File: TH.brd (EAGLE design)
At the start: 129.5 x 71.1 mm, 57 parts, among them IC1 TLE5205-2, IC2 TLE5205-2, IC3 TLE5205-2, IC5 TLE5205-2, J1 I2C, J3 POWERPOLE_DOUBLE, M0 Motor3, M1 Motor3, M2 Motor3, M3 Motor3, U1 LM2576.SMD

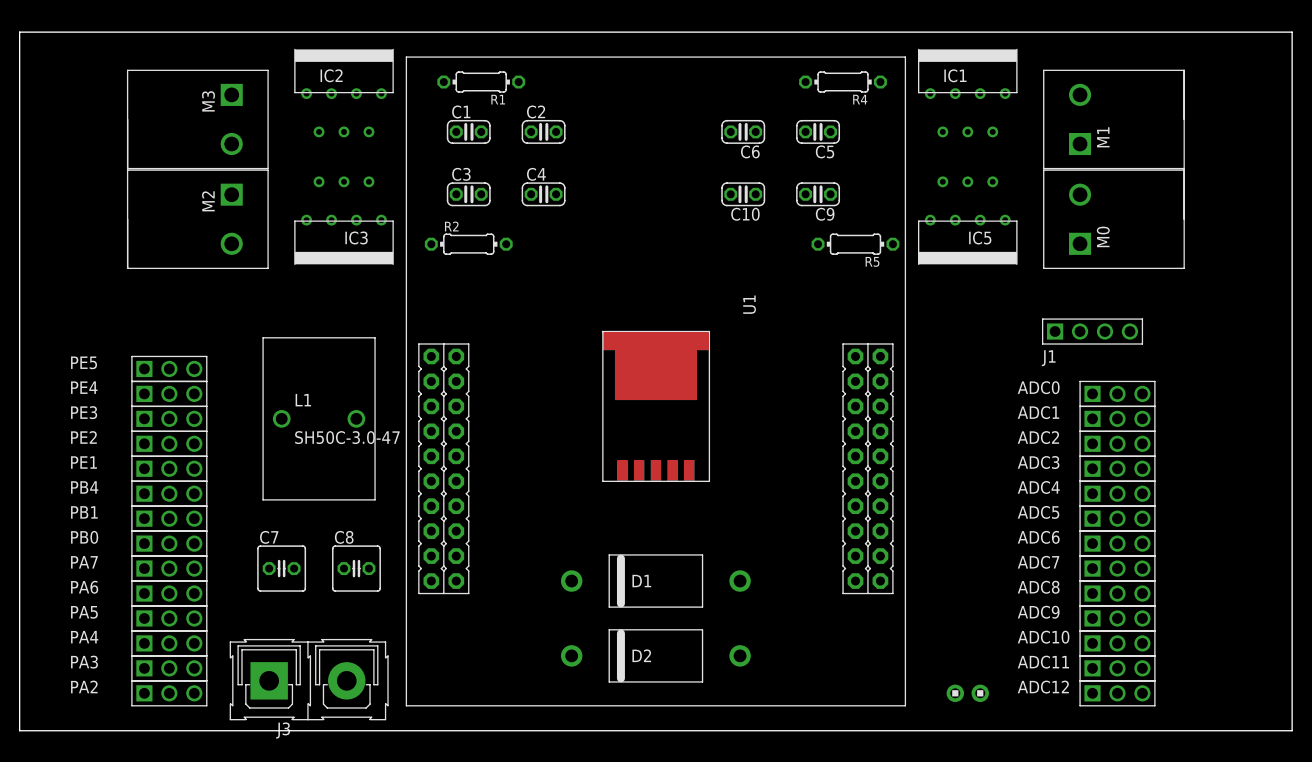
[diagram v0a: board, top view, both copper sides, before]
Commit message: Finished Traces
Only thing left to do is label everything, and ground layer, with do
this tomorrow after TRR
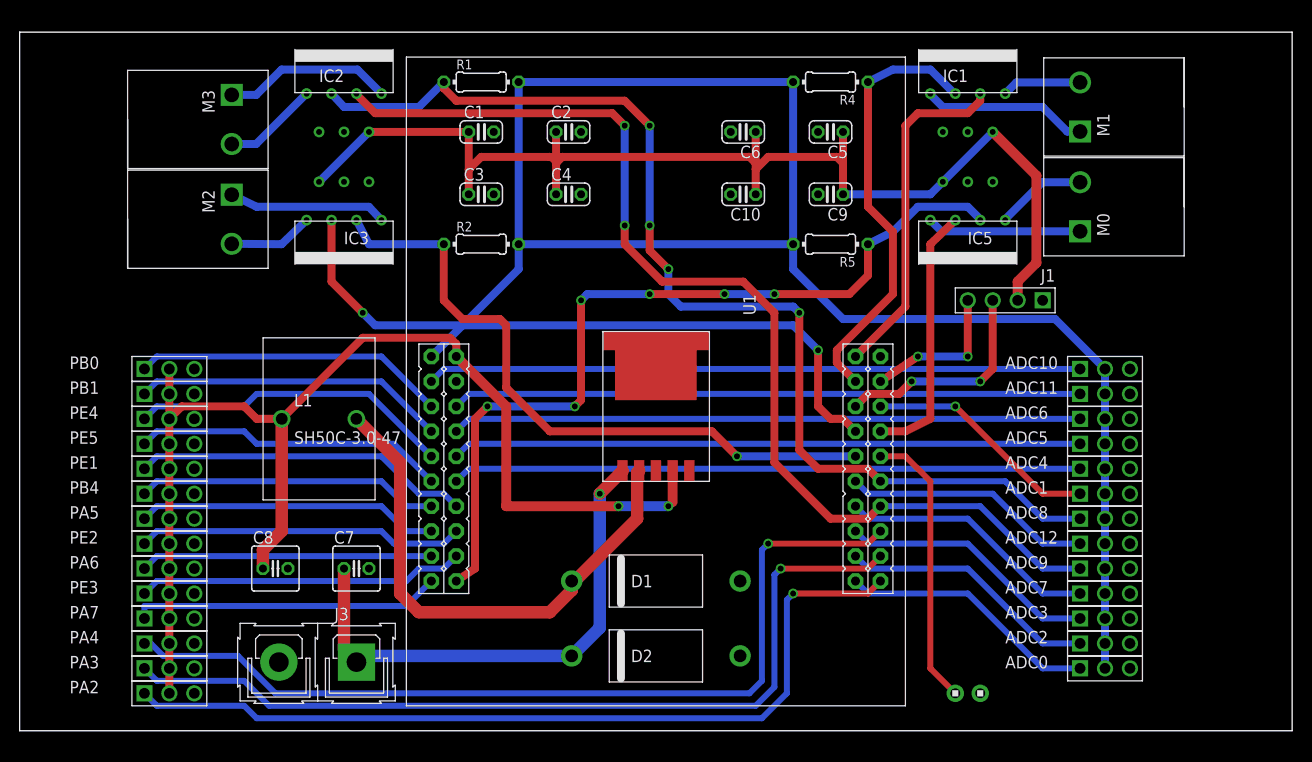
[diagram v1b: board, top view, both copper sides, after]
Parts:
- moved ADC0 28.0 mm to (95.2, 3.81)
- moved ADC11 28.0 mm to (95.2, 31.8)
- moved ADC10 28.0 mm to (95.2, 34.3)
- moved ADC2 20.4 mm to (95.2, 6.35)
- moved PE3 17.8 mm to (0.00, 11.4)
- moved PB0 17.8 mm to (0.00, 34.3)
- moved ADC12 15.3 mm to (95.2, 16.5)
- moved ADC3 15.3 mm to (95.2, 8.89)
- moved ADC6 12.8 mm to (95.2, 29.2)
- moved PB1 12.7 mm to (0.00, 31.8)
- moved PA5 10.2 mm to (0.00, 19.1)
- moved PE2 10.2 mm to (0.00, 16.5)
- moved J1 9.44 mm to (87.6, 41.3), turned to 180 degrees
- moved J3 9.09 mm to (21.6, 4.45), turned to 180 degrees
- moved C8 8.25 mm to (13.3, 14.0)
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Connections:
- removed net -GND: ADC0.3, ADC1.3, ADC10.3, ADC11.3, ADC12.3, ADC2.3, ADC3.3, ADC4.3, ADC5.3, ADC6.3, ADC7.3, ADC8.3, ADC9.3, C1.2, C10.2, C2.2, C3.2, C4.2, C5.2, C6.2, C7.2, C8.2, C9.2, D1.2, D2.2, J3.2, PA2.3, PA3.3, PA4.3, PA5.3, PA6.3, PA7.3, PB0.3, PB1.3, PB4.3, PE1.3, PE2.3, PE3.3, PE4.3, PE5.3, U$1.GND1, U$1.GND2, U$2.2, U1.3, U1.5, U1.GROUND, U1.GROUND@1
- removed net N$10: J1.1
- removed net N$14: ADC11.1
- removed net N$15: ADC12.1
- net GND: now also ADC0.3, ADC1.3, ADC10.3, ADC11.3, ADC12.3, ADC2.3, ADC3.3, ADC4.3, ADC5.3, ADC6.3, ADC7.3, ADC8.3, ADC9.3, C1.2, C10.2, C2.2, C3.2, C4.2, C5.2, C6.2, C7.2, C8.2, C9.2, D1.2, D2.2, IC5.4, J1.1, J3.2, PA2.3, PA3.3, PA4.3, PA5.3, PA6.3, PA7.3, PB0.3, PB1.3, PB4.3, PE1.3, PE2.3, PE3.3, PE4.3, PE5.3, U$1.GND1, U$1.GND2, U$2.2, U1.3, U1.5, U1.GROUND, U1.GROUND@1
- net PC6: now also ADC12.1
- net PD0: now also ADC11.1
- net V+: no longer C1.1, C10.1, C2.1, C3.1, C4.1, C5.1, C6.1, C9.1, IC1.6, IC3.6
- net VBUS: now also C1.1, C10.1, C2.1, C3.1, C4.1, C5.1, C6.1, C9.1, IC1.6, IC2.6, IC3.6, IC5.6
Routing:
- net VBUS: track 0.00 -> 242.5 mm, vias 0 -> 2
- net +3V3: track 0.00 -> 173.6 mm
- net PB7: track 0.00 -> 113.7 mm, vias 0 -> 4
- net PB6: track 0.00 -> 110.8 mm, vias 0 -> 2
- net PA4: track 0.00 -> 91.7 mm, vias 0 -> 1
- net PA3: track 0.00 -> 89.5 mm, vias 0 -> 1
- net PA2: track 0.00 -> 87.3 mm, vias 0 -> 1
- net PF1: track 0.00 -> 86.1 mm, vias 0 -> 6
- net PC4: track 0.00 -> 69.3 mm, vias 0 -> 2
- net PC5: track 0.00 -> 68.3 mm, vias 0 -> 1
- net PB5: track 0.00 -> 66.6 mm
- net PD3: track 0.00 -> 64.0 mm
- net PD2: track 0.00 -> 64.0 mm
- net PD1: track 0.00 -> 64.0 mm
- net PD0: track 0.00 -> 64.0 mm
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
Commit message: Final Design
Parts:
- removed ADC0, ADC3: 3PINHEADER, RASEagleLib:3PINHEADER
- removed M0, M1: Motor3, RASEagleLib:PHOENIXSCREWTERMINAL_2
- added D3: D2, RASEagleLib:DIODE_17MM
- added PF1: PF0, RASEagleLib:PHOENIXSCREWTERMINAL_2
- added PF2: PF3, RASEagleLib:PHOENIXSCREWTERMINAL_2
- added R3, R6: 10K, resistor:0204/7
- PB7: value Motor3 -> PB6
- PC4: value Motor3 -> PC5
- moved PA2 95.6 mm to (95.2, 8.89)
- renumbered ADC1 to PE0, ADC10 to PB5, ADC11 to PD0, ADC12 to PC7, ADC2 to PF4, ADC4 to PD3, ADC5 to PD2, ADC6 to PD1, ADC7 to PD7, ADC8 to PC6, ADC9 to PD6, M2 to PC4, M3 to PB7
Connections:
- removed net +3V3: ADC0.2, ADC3.2, PB5.2, PC6.2, PC7.2, PD0.2, PD1.2, PD2.2, PD3.2, PD6.2, PD7.2, PE0.2, PF4.2, R1.2, R2.2, R4.2, R5.2, U$1.3.3V
- new net 3.3V: J1.2, PA2.2, PB5.2, PC6.2, PC7.2, PD0.2, PD1.2, PD2.2, PD3.2, PD6.2, PD7.2, PE0.2, PF4.2, R3.2, R6.2, U$1.3.3V
- new net N$5$: C8.1, D3.2, L1.P$2, U1.4
- net GND: now also R1.2, R2.2, R4.2, R5.2; no longer ADC0.3, ADC3.3, PA2.3
- net N$12: now also PF1.2; no longer M0.2
- net N$13: now also PF1.1; no longer M0.1
- net N$7: now also PF2.1; no longer M1.1
- net N$8: now also PF2.2; no longer M1.2
- net PB2: now also R6.1
- net PB3: now also R3.1
- net PB6: no longer PD6.1
- net PB7: no longer PC6.1
- net PC6: now also PC6.1; no longer PC7.1
- net PC7: now also PC7.1; no longer PD7.1
- net PD6: now also PD6.1; no longer ADC3.1
- net PD7: now also PD7.1; no longer PF4.1
- net PF4: now also PF4.1; no longer ADC0.1
- net V+: now also C1.1, C10.1, C2.1, C3.1, C4.1, C5.1, C6.1, C9.1, IC1.6, IC2.6, IC3.6, IC5.6
- net VBUS: now also D3.1; no longer C1.1, C10.1, C2.1, C3.1, C4.1, C5.1, C6.1, C8.1, C9.1, IC1.6, IC2.6, IC3.6, IC5.6, J1.2, L1.P$2, PA2.2, U1.4
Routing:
- net +3V3: track 173.6 -> 0.00 mm
- net VBUS: track 242.5 -> 70.5 mm, vias 2 -> 1
- net V+: track 53.2 -> 203.4 mm, vias 1 -> 3
- net 3.3V: track 0.00 -> 123.2 mm
- net N$5$: track 0.00 -> 73.3 mm, vias 0 -> 2
- net PA2: track 87.3 -> 21.9 mm, vias 1 -> 0
- net PB6: track 110.8 -> 87.8 mm
- net PB7: track 113.7 -> 91.9 mm
- net PB3: track 22.5 -> 24.6 mm
- net PD6: track 26.5 -> 24.4 mm
- net PC7: track 26.5 -> 24.4 mm
- net PD7: track 26.5 -> 24.4 mm
- net N$13: track 15.7 -> 17.5 mm
- net N$7: track 16.9 -> 18.7 mm
- net PD0: track 64.0 -> 65.1 mm, vias 0 -> 2
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- added copper zone on layer 1, net GND
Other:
- board size 129.5 x 71.1 mm -> 118.7 x 72.4 mm
- board text added: "3.3V"
- board text added: "5V"
- board text added: "GND"
- board text added: "Stellaris LaunchPad"
